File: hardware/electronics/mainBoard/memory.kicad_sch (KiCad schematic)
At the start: 0 parts

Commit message: added external memory sch
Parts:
- added C31, C32, C33: 100nF, symbol lib_sch:C
- added J1: MEM2067-02-180-00-A, symbol lib_sch:microSD
- added U3: W25Q128JVP, symbol lib_sch:W25Q128JVP
- added U4: M24512-DRE, symbol lib_sch:M24512-DRE
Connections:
- new net +3V3: C31.1, C32.1, C33.1, J1.4 (VDD), U3.8 (VCC), U4.8 (VCC)
- new net EEPROM_WC: U4.7 (~{WC})
- new net I2C1.SCL: U4.6 (SCL)
- new net I2C1.SDA: U4.5 (SDA)
- new net QSPI1.CLK: U3.6 (SCK)
- new net QSPI1.IO0: U3.5 (DI)
- new net QSPI1.IO1: U3.2 (DO)
- new net QSPI1.IO2: U3.3 (~{WP})
- new net QSPI1.IO3: U3.7 (~{HOLD})
- new net QSPI1.NCS: U3.1 (~{CS})
- new net SDMMC2.CLK: J1.5 (CLK)
- new net SDMMC2.CMD: J1.3 (CMD)
- new net SDMMC2.D0: J1.7 (DAT0)
- new net SDMMC2.D1: J1.8 (DAT1)
- new net SDMMC2.D2: J1.1 (DAT2)
- new net SDMMC2.D3: J1.2 (DAT3/CD)
- new net VSS: C31.2, C32.2, C33.2, J1.11 (SHIELD), J1.6 (VSS), U3.4 (GND), U3.9 (GND_PAD), U4.1 (E0), U4.2 (E1), U4.3 (E2), U4.4 (VSS)
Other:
- note added: "I2C Address: 0x50/0x58"
- title: (none) -> Memory

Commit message: fixed power flags
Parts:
- renumbered J1 to J2

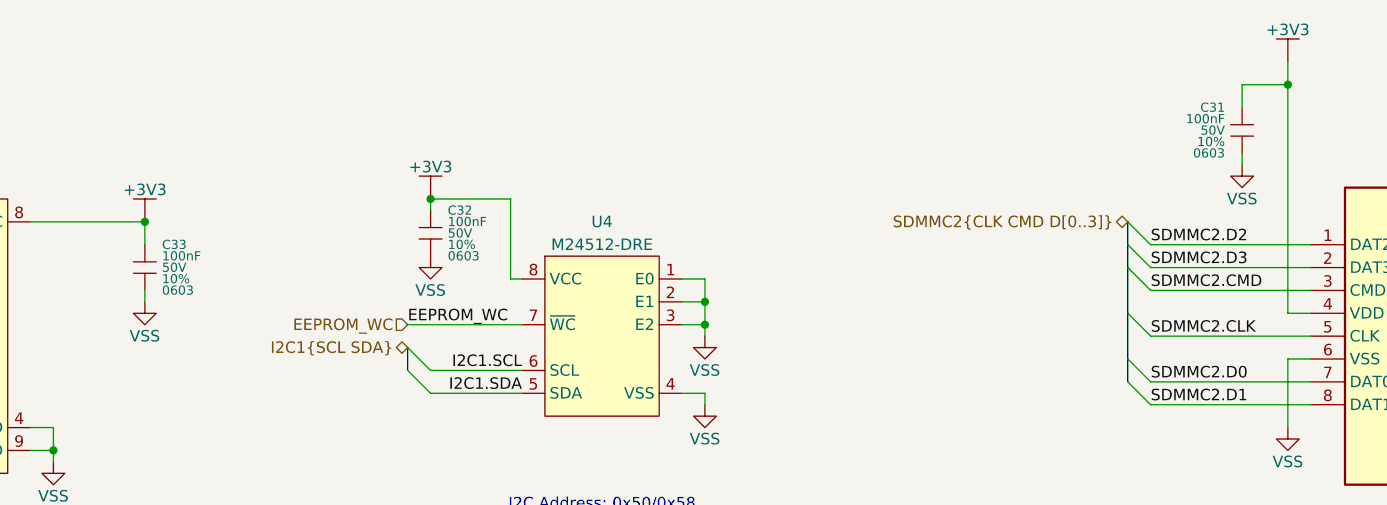
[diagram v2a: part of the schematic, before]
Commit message: updated capacitors
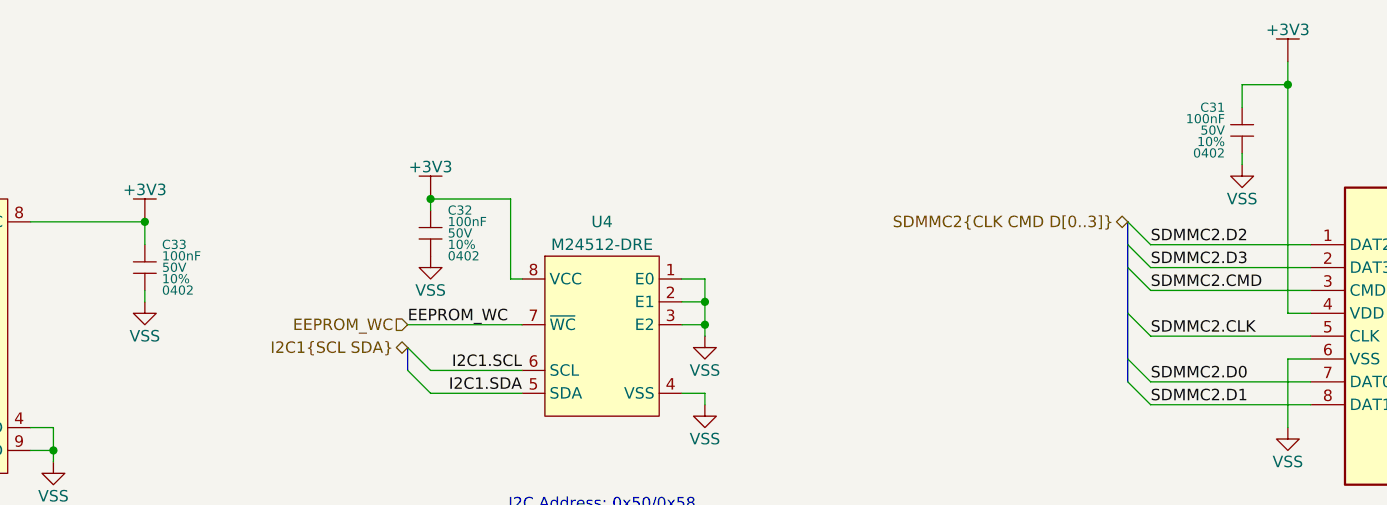
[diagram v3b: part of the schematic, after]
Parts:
- C31, C32, C33: DKPN 478-KAM15AR71H104KTCT-ND -> 490-GRT155R71H104KE01DCT-ND; MPN 06035C104K4T2A -> GRT155R71H104KE01D; Manufacturer KYOCERA AVX -> Murata Electronics; Package 0603 -> 0402
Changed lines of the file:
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@@
+			)
+		)
+		(property "Frequency" ""
+			(at 241.3 107.95 0)
+			(effects
+				(font
+					(size 1.27 1.27)
+				)
+			)
+		)
+		(property "Tolerace" ""
+			(at 241.3 107.95 0)
+			(effects
+				(font
+					(size 1.27 1.27)
+				)
+			)
+		)
+		(property "Trip Current" ""
+			(at 241.3 107.95 0)
+			(effects
+				(font
+					(size 1.27 1.27)
+				)
+			)
+		)
+		(property "Voltage" ""
+			(at 241.3 107.95 0)
+			(effects
+				(font
+					(size 1.27 1.27)
+				)
 			)
 		)
@@
 			)
 		)
-		(property "Datasheet" "datasheets/KYOCERA-AVX-MLCCKAM.pdf"
+		(property "Datasheet" "datasheets/Murata-Electronics-GRT155R71H104KE01.pdf"
 			(at 210.82 83.185 0)
 			(effects
@@
 			)
 		)
-		(property "Description" "CAP CER 0.1UF 50V X7R 0603"
+		(property "Description" "CAP CER 0.1UF 50V X7R 0402"
 			(at 210.82 85.09 0)
 			(effects
@@
 			)
 		)
-		(property "Manufacturer" "KYOCERA AVX"
+		(property "Manufacturer" "Murata Electronics"
 			(at 210.82 83.185 0)
 			(effects
@@
 			)
 		)
-		(property "MPN" "06035C104K4T2A"
+		(property "MPN" "GRT155R71H104KE01D"
 			(at 210.82 83.185 0)
 			(effects
@@
 			)
 		)
-		(property "DKPN" "478-KAM15AR71H104KTCT-ND"
+		(property "DKPN" "490-GRT155R71H104KE01DCT-ND"
 			(at 210.82 85.09 0)
 			(effects
@@
 			)
 		)
-		(property "Package" "0603"
+		(property "Package" "0402"
 			(at 208.915 87.63 0)
 			(do_not_autoplace yes)
@@
 				)
 				(justify left)
+			)
+		)
+		(property "Frequency" ""
+			(at 210.82 85.09 0)
+			(effects
+				(font
+					(size 1.27 1.27)
+				)
+			)
+		)
+		(property "Tolerace" ""
+			(at 210.82 85.09 0)
+			(effects
+				(font
+					(size 1.27 1.27)
+				)
+			)
+		)
+		(property "Trip Current" ""
+			(at 210.82 85.09 0)
+			(effects
+				(font
+					(size 1.27 1.27)
+				)
+			)
+		)
+		(property "Voltage" ""
+			(at 210.82 85.09 0)
+			(effects
+				(font
+					(size 1.27 1.27)
+				)
 			)
 		)
@@
 			)
 		)
-		(property "Datasheet" "datasheets/KYOCERA-AVX-MLCCKAM.pdf"
+		(property "Datasheet" "datasheets/Murata-Electronics-GRT155R71H104KE01.pdf"
 			(at 120.65 94.615 0)
 			(effects
@@
 			)
 		)
-		(property "Description" "CAP CER 0.1UF 50V X7R 0603"
+		(property "Description" "CAP CER 0.1UF 50V X7R 0402"
 			(at 120.65 96.52 0)
 			(effects
@@
 			)
 		)
-		(property "Manufacturer" "KYOCERA AVX"
+		(property "Manufacturer" "Murata Electronics"
 			(at 120.65 94.615 0)
 			(effects
@@
 			)
 		)
-		(property "MPN" "06035C104K4T2A"
+		(property "MPN" "GRT155R71H104KE01D"
 			(at 120.65 94.615 0)
 			(effects
@@
 			)
 		)
-		(property "DKPN" "478-KAM15AR71H104KTCT-ND"
+		(property "DKPN" "490-GRT155R71H104KE01DCT-ND"
 			(at 120.65 96.52 0)
 			(effects
@@
 			)
 		)
-		(property "Package" "0603"
+		(property "Package" "0402"
 			(at 122.555 99.06 0)
 			(do_not_autoplace yes)
@@
 				)
 				(justify left)
+			)
+		)
+		(property "Frequency" ""
+			(at 120.65 96.52 0)
+			(effects
+				(font
+					(size 1.27 1.27)
+				)
+			)
+		)
+		(property "Tolerace" ""
+			(at 120.65 96.52 0)
+			(effects
+				(font
+					(size 1.27 1.27)
+				)
+			)
+		)
+		(property "Trip Current" ""
+			(at 120.65 96.52 0)
+			(effects
+				(font
+					(size 1.27 1.27)
+				)
+			)
+		)
+		(property "Voltage" ""
+			(at 120.65 96.52 0)
+			(effects
+				(font
+					(size 1.27 1.27)
+				)
 			)
 		)
@@
 			)
 		)
-		(property "Datasheet" "datasheets/KYOCERA-AVX-MLCCKAM.pdf"
+		(property "Datasheet" "datasheets/Murata-Electronics-GRT155R71H104KE01.pdf"
 			(at 88.9 98.425 0)
 			(effects
@@
 			)
 		)
-		(property "Description" "CAP CER 0.1UF 50V X7R 0603"
+		(property "Description" "CAP CER 0.1UF 50V X7R 0402"
 			(at 88.9 100.33 0)
 			(effects
@@
 			)
 		)
-		(property "Manufacturer" "KYOCERA AVX"
+		(property "Manufacturer" "Murata Electronics"
 			(at 88.9 98.425 0)
 			(effects
@@
 			)
 		)
-		(property "MPN" "06035C104K4T2A"
+		(property "MPN" "GRT155R71H104KE01D"
 			(at 88.9 98.425 0)
 			(effects
@@
 			)
 		)
-		(property "DKPN" "478-KAM15AR71H104KTCT-ND"
+		(property "DKPN" "490-GRT155R71H104KE01DCT-ND"
 			(at 88.9 100.33 0)
 			(effects
@@
 			)
 		)
-		(property "Package" "0603"
+		(property "Package" "0402"
 			(at 90.805 102.87 0)
 			(do_not_autoplace yes)
@@
 				)
 				(justify left)
+			)
+		)
+		(property "Frequency" ""
+			(at 88.9 100.33 0)
+			(effects
+				(font
+					(size 1.27 1.27)
+				)
+			)
+		)
+		(property "Tolerace" ""
+			(at 88.9 100.33 0)
+			(effects
+				(font
+					(size 1.27 1.27)
+				)
+			)
+		)
+		(property "Trip Current" ""
+			(at 88.9 100.33 0)
+			(effects
+				(font
+					(size 1.27 1.27)
+				)
+			)
+		)
+		(property "Voltage" ""
+			(at 88.9 100.33 0)
+			(effects
+				(font
+					(size 1.27 1.27)
+				)
 			)
 		)
@@
 			)
 		)
+		(property "Frequency" ""
+			(at 63.5 107.95 0)
+			(effects
+				(font
+					(size 1.27 1.27)
+				)
+			)
+		)
+		(property "Tolerace" ""
+			(at 63.5 107.95 0)
+			(effects
+				(font
+					(size 1.27 1.27)
+				)
+			)
+		)
+		(property "Trip Current" ""
+			(at 63.5 107.95 0)
+			(effects
+				(font
+					(size 1.27 1.27)
+				)
+			)
+		)
+		(property "Voltage" ""
+			(at 63.5 107.95 0)
+			(effects
+				(font
+					(size 1.27 1.27)
+				)
+			)
+		)
 		(pin "1"
 		)
@@
 			)
 		)
+		(property "Frequency" ""
+			(at 139.7 107.95 0)
+			(effects
+				(font
+					(size 1.27 1.27)
+				)
+			)
+		)
+		(property "Tolerace" ""
+			(at 139.7 107.95 0)
+			(effects
+				(font
+					(size 1.27 1.27)
+				)
+			)
+		)
+		(property "Trip Current" ""
+			(at 139.7 107.95 0)
+			(effects
+				(font
+					(size 1.27 1.27)
+				)
+			)
+		)
+		(property "Voltage" ""
+			(at 139.7 107.95 0)
+			(effects
+				(font
+					(size 1.27 1.27)
+				)
+			)
+		)

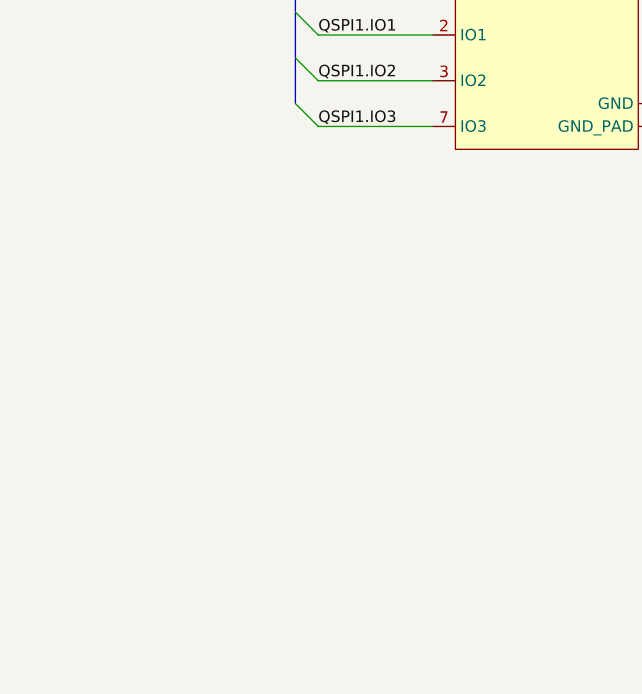
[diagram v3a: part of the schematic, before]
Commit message: added testpoints
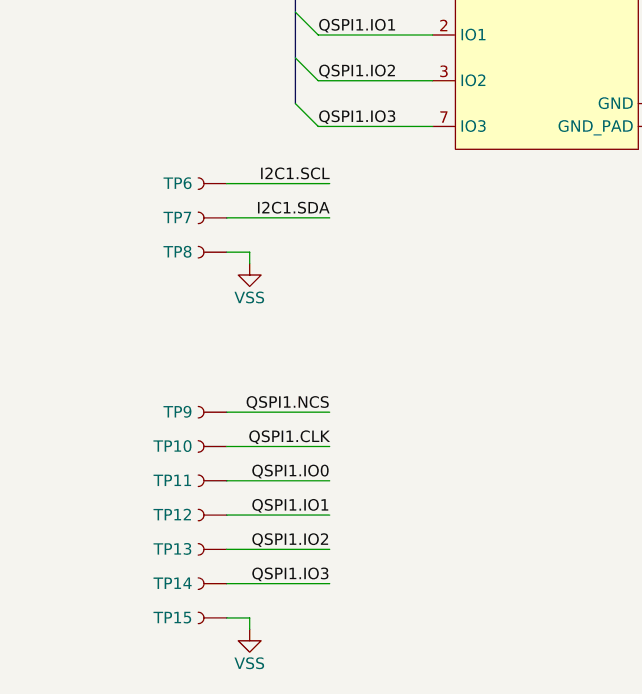
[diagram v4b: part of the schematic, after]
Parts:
- added TP10, TP11, TP12, TP13, TP14, TP6, TP7, TP9: ~, symbol lib_sch:Testpoint
- added TP15, TP8: RCWCTE, symbol lib_sch:Testpoint
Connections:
- net I2C1.SCL: now also TP6.1
- net I2C1.SDA: now also TP7.1
- net QSPI1.CLK: now also TP10.1
- net QSPI1.IO0: now also TP11.1
- net QSPI1.IO1: now also TP12.1
- net QSPI1.IO2: now also TP13.1
- net QSPI1.IO3: now also TP14.1
- net QSPI1.NCS: now also TP9.1
- net VSS: now also TP15.1, TP8.1

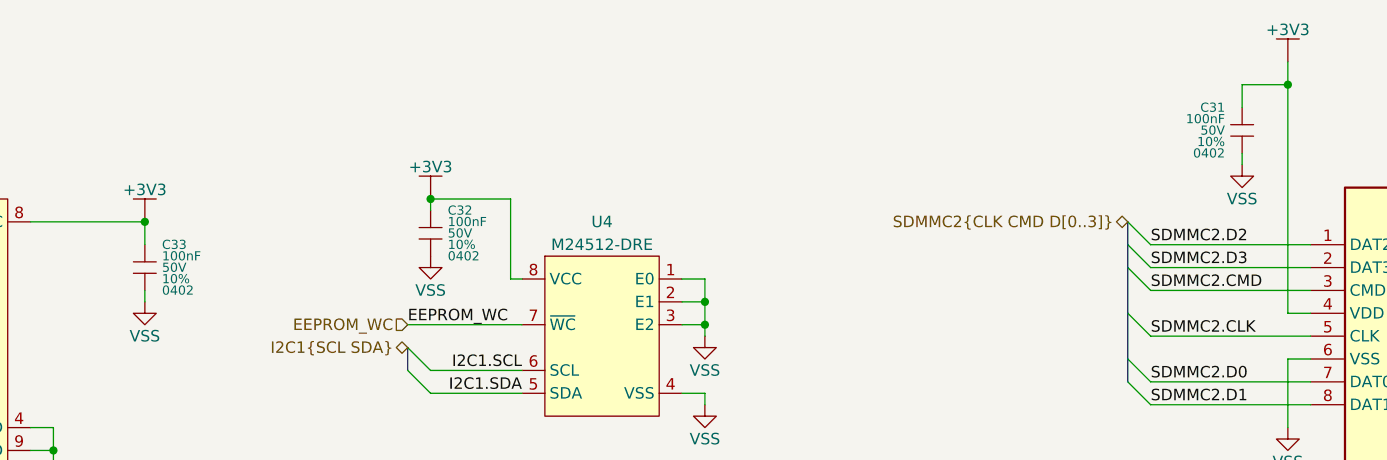
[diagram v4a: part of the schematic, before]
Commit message: updated symbol refs
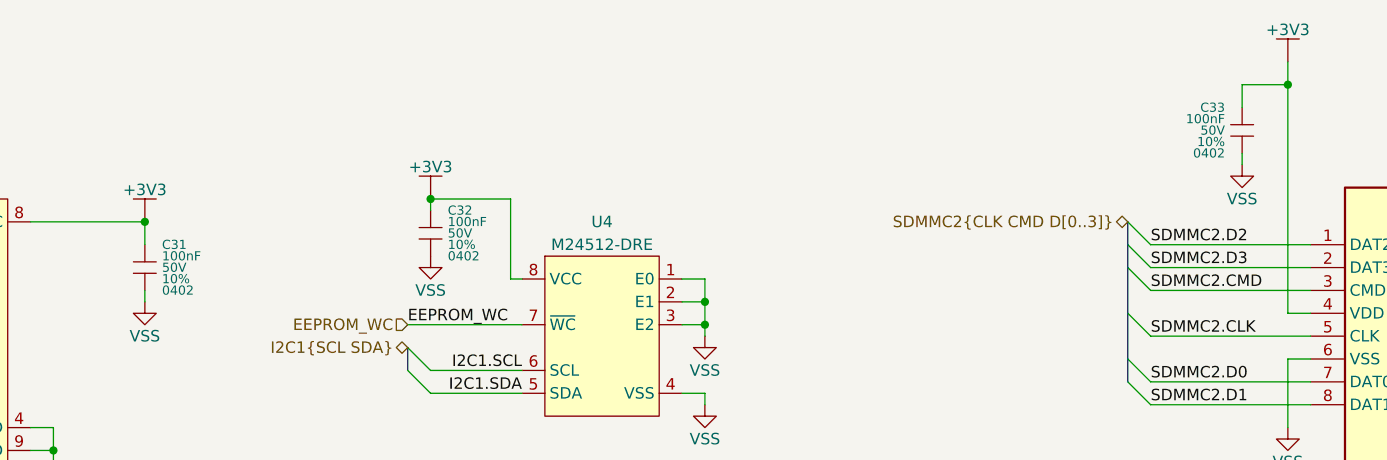
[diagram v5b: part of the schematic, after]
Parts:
- renumbered C33 to C31, C31 to C33
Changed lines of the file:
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@@
 		(dnp no)
 		(fields_autoplaced yes)
-		(property "Reference" "#PWR067"
+		(property "Reference" "#PWR068"
 			(at 88.9 95.25 0)
 			(effects
@@
 			(project ""
 				(path "/be16e32f-2ccf-4272-9ec7-94d5fe7a55e0/bf9ac865-aa9a-42a1-8ada-6ec99a5fbf41"
-					(reference "#PWR067")
+					(reference "#PWR068")
 					(unit 1)
 				)
@@
 		(dnp no)
 		(fields_autoplaced yes)
-		(property "Reference" "#PWR066"
+		(property "Reference" "#PWR070"
 			(at 120.65 92.71 0)
 			(effects
@@
 			(project "mainBoard"
 				(path "/be16e32f-2ccf-4272-9ec7-94d5fe7a55e0/bf9ac865-aa9a-42a1-8ada-6ec99a5fbf41"
-					(reference "#PWR066")
+					(reference "#PWR070")
 					(unit 1)
 				)
@@
 		(on_board yes)
 		(dnp no)
-		(property "Reference" "C31"
+		(property "Reference" "C33"
 			(at 208.915 82.55 0)
 			(do_not_autoplace yes)
@@
 			(project "mainBoard"
 				(path "/be16e32f-2ccf-4272-9ec7-94d5fe7a55e0/bf9ac865-aa9a-42a1-8ada-6ec99a5fbf41"
-					(reference "C31")
+					(reference "C33")
 					(unit 1)
 				)
@@
 		(dnp no)
 		(fields_autoplaced yes)
-		(property "Reference" "#PWR074"
+		(property "Reference" "#PWR077"
 			(at 264.16 121.92 0)
 			(effects
@@
 			(project "mainBoard"
 				(path "/be16e32f-2ccf-4272-9ec7-94d5fe7a55e0/bf9ac865-aa9a-42a1-8ada-6ec99a5fbf41"
-					(reference "#PWR074")
+					(reference "#PWR077")
 					(unit 1)
 				)
@@
 		(dnp no)
 		(fields_autoplaced yes)
-		(property "Reference" "#PWR072"
+		(property "Reference" "#PWR076"
 			(at 215.9 118.11 0)
 			(effects
@@
 			(project "mainBoard"
 				(path "/be16e32f-2ccf-4272-9ec7-94d5fe7a55e0/bf9ac865-aa9a-42a1-8ada-6ec99a5fbf41"
-					(reference "#PWR072")
+					(reference "#PWR076")
 					(unit 1)
 				)
@@
 		(dnp no)
 		(fields_autoplaced yes)
-		(property "Reference" "C33"
+		(property "Reference" "C31"
 			(at 90.805 97.79 0)
 			(do_not_autoplace yes)
@@
 			(project "mainBoard"
 				(path "/be16e32f-2ccf-4272-9ec7-94d5fe7a55e0/bf9ac865-aa9a-42a1-8ada-6ec99a5fbf41"
-					(reference "C33")
+					(reference "C31")
 					(unit 1)
 				)
@@
 		(dnp no)
 		(fields_autoplaced yes)
-		(property "Reference" "#PWR076"
+		(property "Reference" "#PWR066"
 			(at 30.48 176.53 0)
 			(effects
@@
 			(project "mainBoard"
 				(path "/be16e32f-2ccf-4272-9ec7-94d5fe7a55e0/bf9ac865-aa9a-42a1-8ada-6ec99a5fbf41"
-					(reference "#PWR076")
+					(reference "#PWR066")
 					(unit 1)
 				)
@@
 		(dnp no)
 		(fields_autoplaced yes)
-		(property "Reference" "#PWR071"
+		(property "Reference" "#PWR073"
 			(at 151.13 115.57 0)
 			(effects
@@
 			(project "mainBoard"
 				(path "/be16e32f-2ccf-4272-9ec7-94d5fe7a55e0/bf9ac865-aa9a-42a1-8ada-6ec99a5fbf41"
-					(reference "#PWR071")
+					(reference "#PWR073")
 					(unit 1)
 				)
@@
 		(dnp no)
 		(fields_autoplaced yes)
-		(property "Reference" "#PWR065"
+		(property "Reference" "#PWR074"
 			(at 210.82 88.9 0)
 			(effects
@@
 			(project "mainBoard"
 				(path "/be16e32f-2ccf-4272-9ec7-94d5fe7a55e0/bf9ac865-aa9a-42a1-8ada-6ec99a5fbf41"
-					(reference "#PWR065")
+					(reference "#PWR074")
 					(unit 1)
 				)
@@
 		(dnp no)
 		(fields_autoplaced yes)
-		(property "Reference" "#PWR064"
+		(property "Reference" "#PWR075"
 			(at 215.9 77.47 0)
 			(effects
@@
 			(project "mainBoard"
 				(path "/be16e32f-2ccf-4272-9ec7-94d5fe7a55e0/bf9ac865-aa9a-42a1-8ada-6ec99a5fbf41"
-					(reference "#PWR064")
+					(reference "#PWR075")
 					(unit 1)
 				)
@@
 		(dnp no)
 		(fields_autoplaced yes)
-		(property "Reference" "#PWR075"
+		(property "Reference" "#PWR065"
 			(at 30.48 135.89 0)
 			(effects
@@
 			(project "mainBoard"
 				(path "/be16e32f-2ccf-4272-9ec7-94d5fe7a55e0/bf9ac865-aa9a-42a1-8ada-6ec99a5fbf41"
-					(reference "#PWR075")
+					(reference "#PWR065")
 					(unit 1)
 				)
@@
 		(dnp no)
 		(fields_autoplaced yes)
-		(property "Reference" "#PWR073"
+		(property "Reference" "#PWR067"
 			(at 78.74 121.92 0)
 			(effects
@@
 			(project ""
 				(path "/be16e32f-2ccf-4272-9ec7-94d5fe7a55e0/bf9ac865-aa9a-42a1-8ada-6ec99a5fbf41"
-					(reference "#PWR073")
+					(reference "#PWR067")
 					(unit 1)
 				)
@@
 		(dnp no)
 		(fields_autoplaced yes)
-		(property "Reference" "#PWR070"
+		(property "Reference" "#PWR072"
 			(at 151.13 107.95 0)
 			(effects
@@
 			(project "mainBoard"
 				(path "/be16e32f-2ccf-4272-9ec7-94d5fe7a55e0/bf9ac865-aa9a-42a1-8ada-6ec99a5fbf41"
-					(reference "#PWR070")
+					(reference "#PWR072")
 					(unit 1)
 				)
@@
 		(dnp no)
 		(fields_autoplaced yes)
-		(property "Reference" "#PWR068"
+		(property "Reference" "#PWR071"
 			(at 120.65 99.06 0)
 			(effects
@@
 			(project "mainBoard"
 				(path "/be16e32f-2ccf-4272-9ec7-94d5fe7a55e0/bf9ac865-aa9a-42a1-8ada-6ec99a5fbf41"
-					(reference "#PWR068")
-					(unit 1)
-				)
+					(reference "#PWR071")
+					(unit 1)
+				)
